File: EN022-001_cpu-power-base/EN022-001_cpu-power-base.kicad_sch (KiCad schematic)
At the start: 25 parts, among them J1 MEGA BOTTOM, J10 GBA_Slot, J3 CART SLOT TOP ROW, J4 CART SLOT FRONT ROW, J6 5V USB, J7 Conn_01x07, J8 EXP2, J9 EXP1, M2_1 Screw_Terminal_01x01, M2_2 Screw_Terminal_01x01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

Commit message: applied page layout
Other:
- company: (none) -> iperkeno
- title: OSCR HW5 -> Base board with CPU nad power supply
- moved on the sheet: C1, D1, R1, SW1, SW2

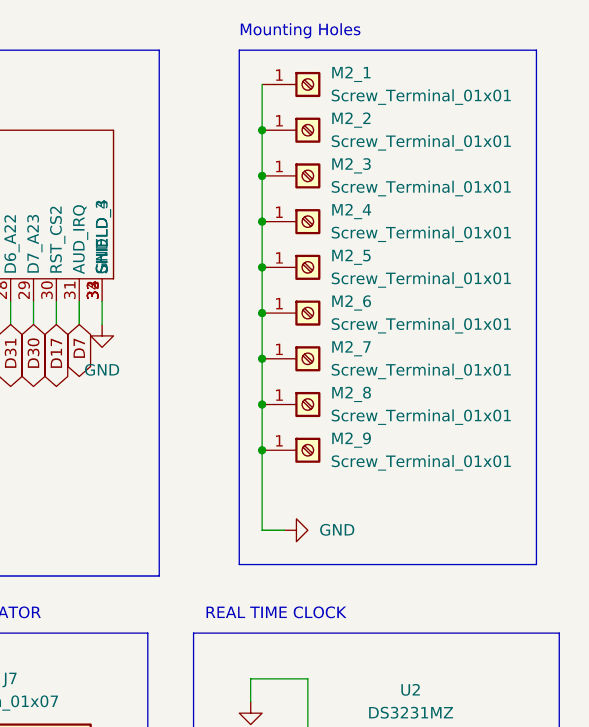
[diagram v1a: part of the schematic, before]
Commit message: mountin holes position
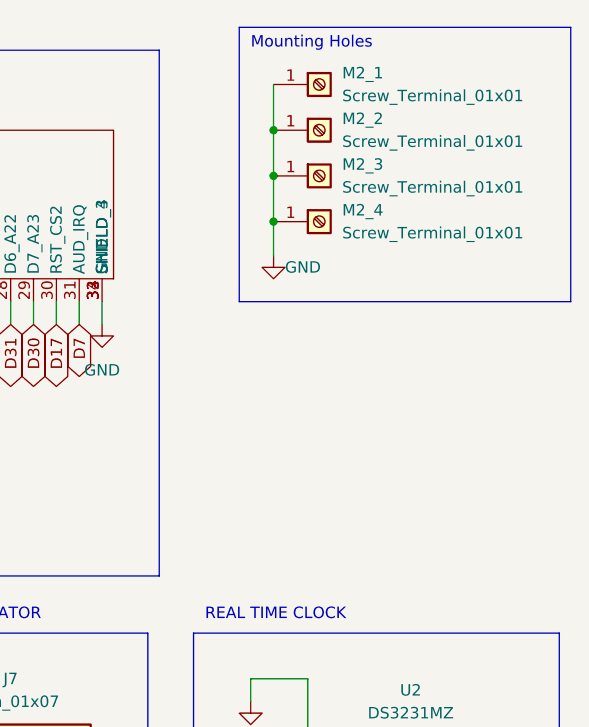
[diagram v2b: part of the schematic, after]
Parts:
- removed M2_5, M2_6, M2_7, M2_8, M2_9: Screw_Terminal_01x01, symbol Connector:Screw_Terminal_01x01
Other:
- moved on the sheet: M2_1, M2_2, M2_3, M2_4

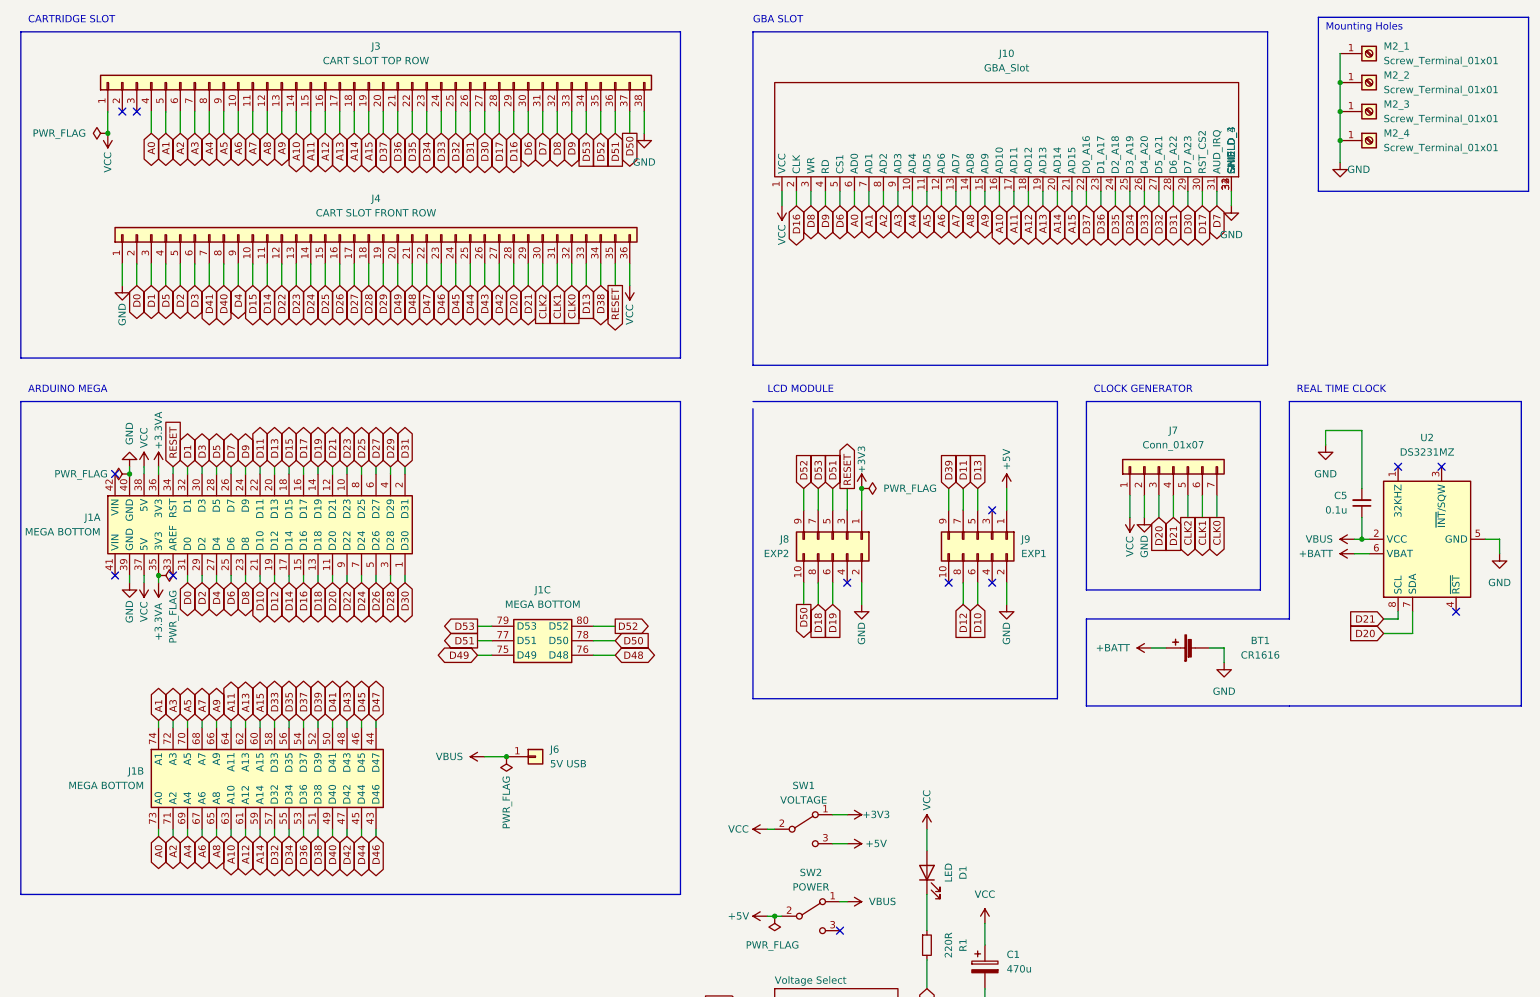
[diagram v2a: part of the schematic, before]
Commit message: Removed atmega board connector
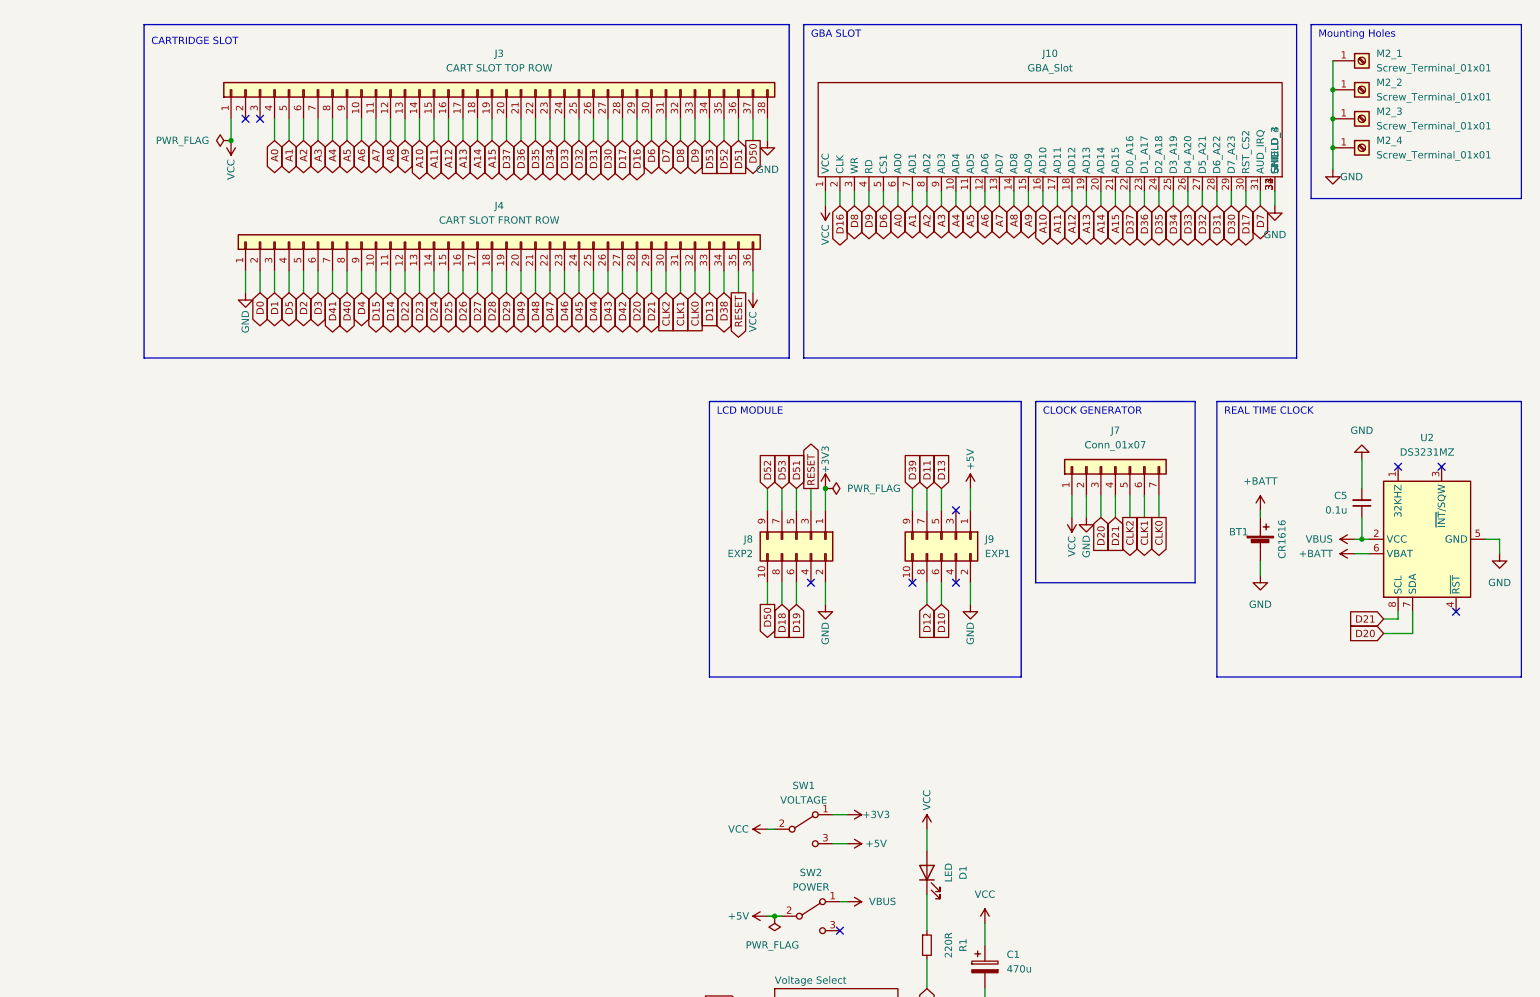
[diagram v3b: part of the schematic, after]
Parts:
- removed J1: MEGA BOTTOM, !OSCR:MEGA2560_PRO_MINI, symbol !OSCR:MEGA2650_PRO_MINI
- removed J6: 5V USB, Connector_PinHeader_2.54mm:PinHeader_1x01_P2.54mm_Vertical, symbol Connector_Generic:Conn_01x01
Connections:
- no-connect marks 13 -> 10
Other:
- note removed: "ARDUINO MEGA"
- moved on the sheet: BT1, J10, J3, J4, J7, J8, J9, M2_1, M2_2, M2_3, M2_4

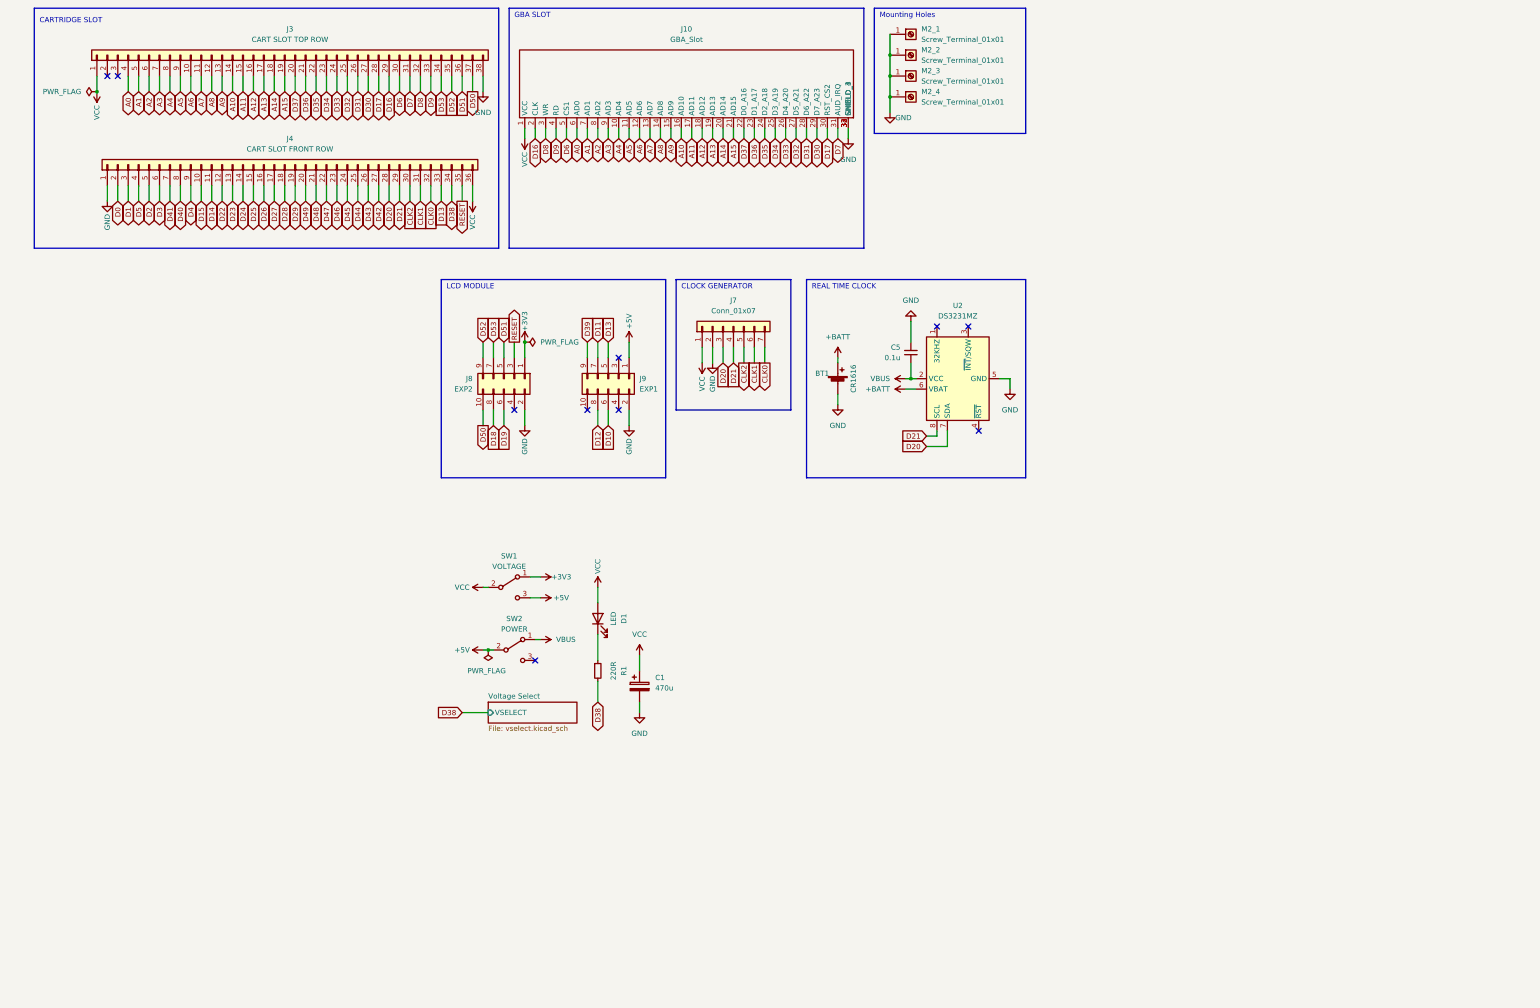
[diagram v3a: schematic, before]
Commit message: updateted GBA slot
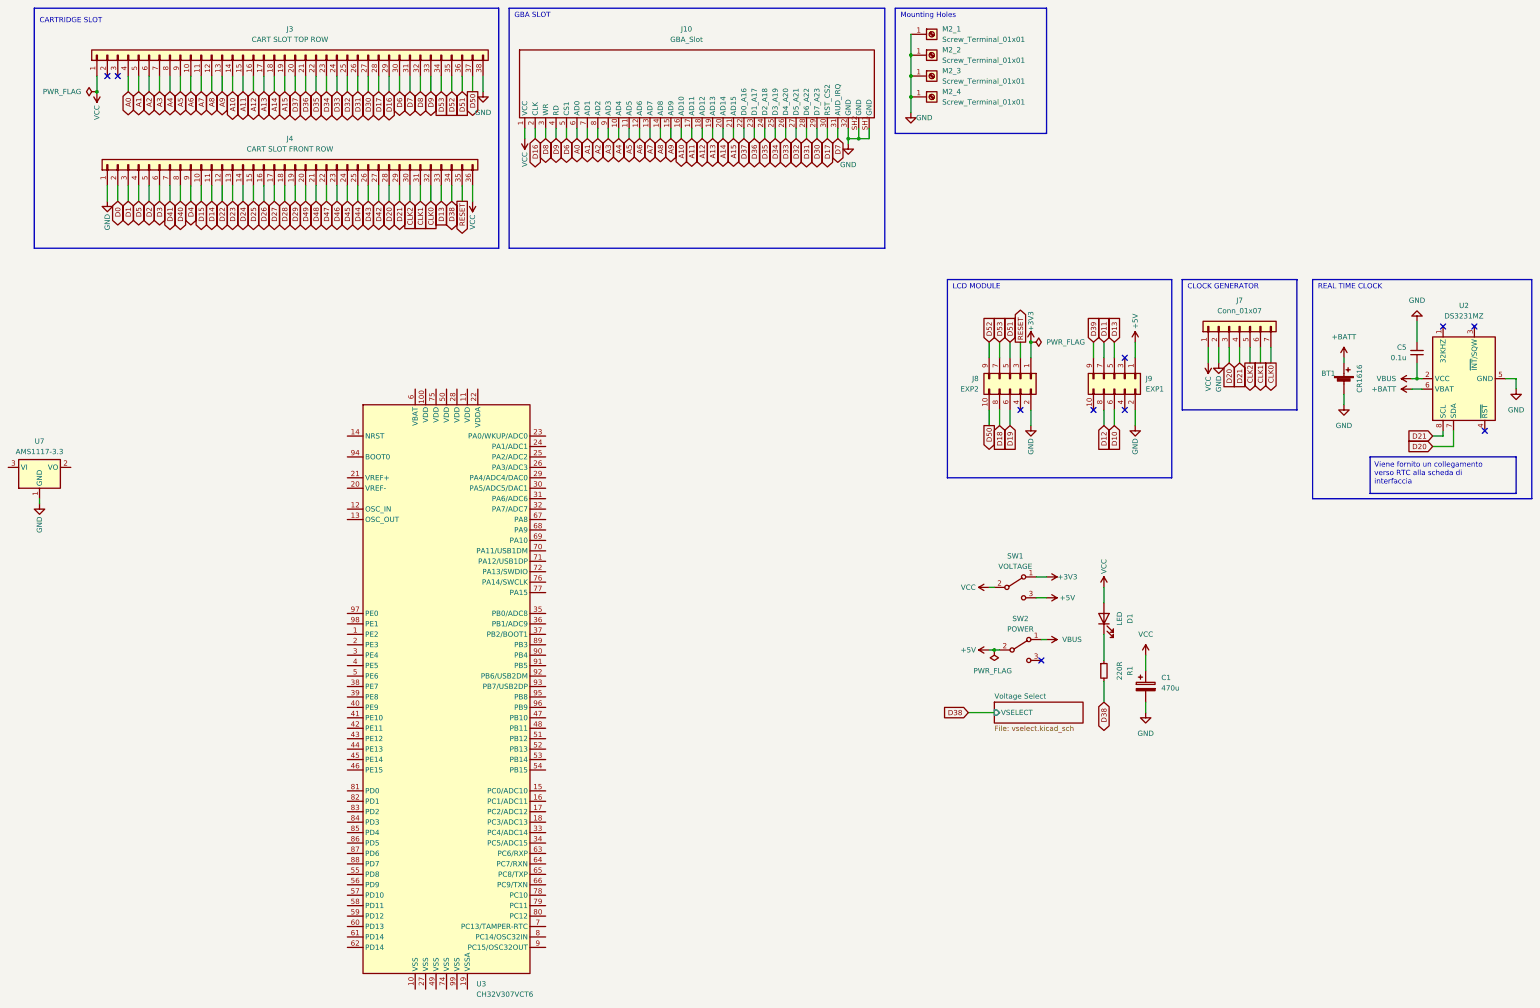
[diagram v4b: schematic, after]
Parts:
- added U3: CH32V307VCT6, Package_QFP:LQFP-100_14x14mm_P0.5mm, symbol wch-mcu:CH32V307VCT6
- added U7: AMS1117-3.3, Package_TO_SOT_SMD:SOT-223-3_TabPin2, symbol Regulator_Linear:AMS1117-3.3
- J10: footprint (none) -> !OSCR:GBA_Slot
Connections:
- net GND: now also J10.SH1 (GND), J10.SH2 (GND), U7.1 (GND); no longer J10.33 (SHIELD_3), J10.34 (SHIELD_4)
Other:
- moved on the sheet: BT1, C1, C5, D1, J7, J8, J9, M2_1, M2_2, M2_3, M2_4, R1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
